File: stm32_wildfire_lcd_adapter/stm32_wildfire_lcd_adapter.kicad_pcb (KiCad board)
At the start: 2 copper layers, 30 x 30 mm, 3 parts, among them J1 Wildfire_40P_LCD, J2 STM32_40_LCD

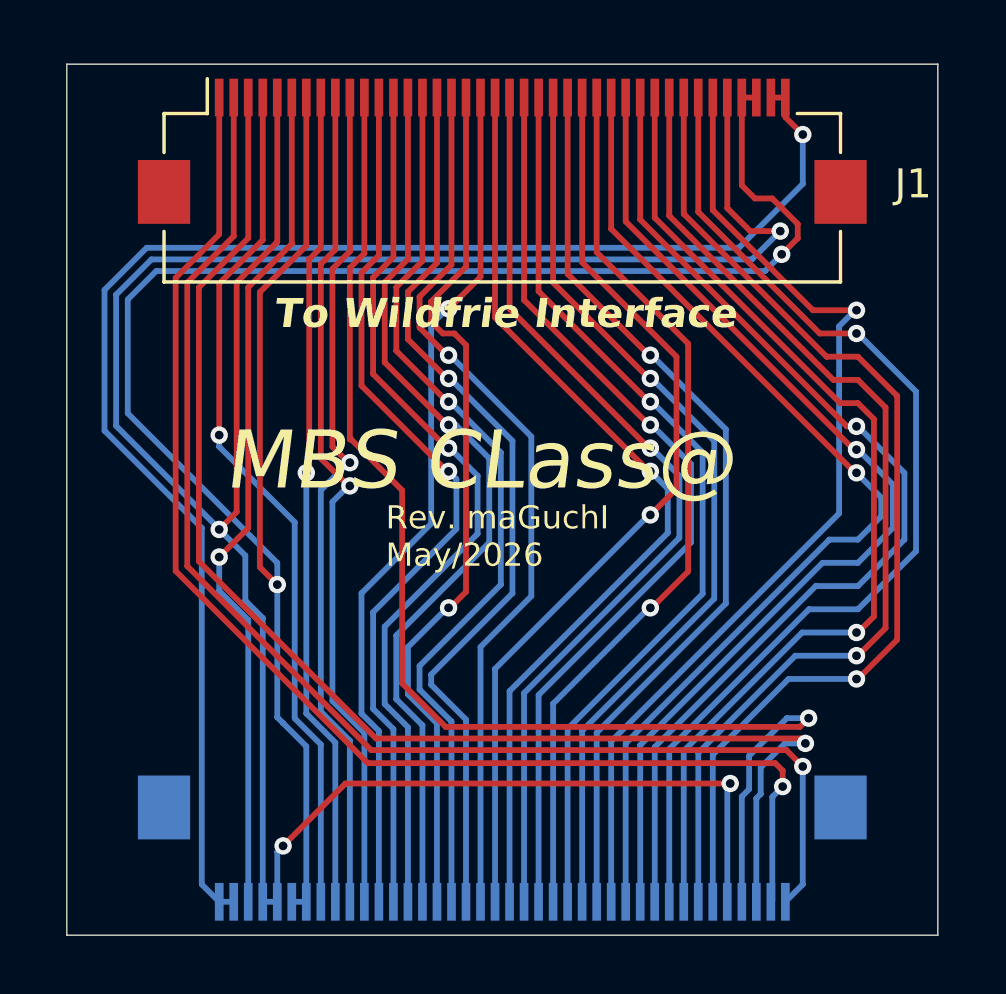
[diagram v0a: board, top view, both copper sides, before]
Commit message: fixing pinout error from wrong manual
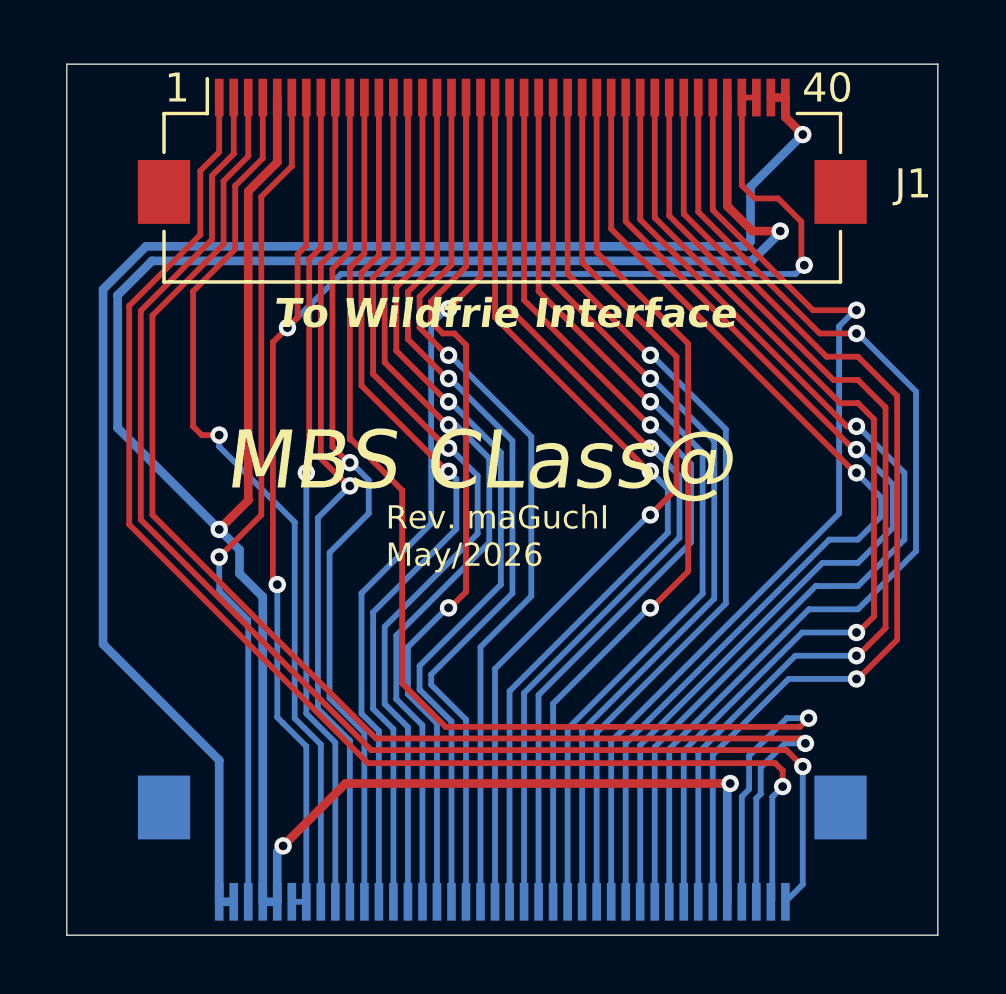
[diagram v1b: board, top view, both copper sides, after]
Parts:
- removed REF**: OSHW-Logo2_14.6x12mm_SilkScreen, Symbol:OSHW-Logo2_14.6x12mm_SilkScreen
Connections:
- J1 pad 10: /LCD_VSYNC -> /LCD_HSYNC
- J1 pad 9: /LCD_HSYNC -> /LCD_VSYNC
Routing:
- net /3V3: track 71.9 -> 55.5 mm, vias 2 -> 3
- net /CTP_SCL: track 45.4 -> 46.7 mm
- net /CTP_SDA: track 45.8 -> 47.1 mm
- net /CTP_INT: track 46.7 -> 48.1 mm
- net /CTP_RST: track 29.8 -> 30.9 mm
- net /LCD_HSYNC: track 29.1 -> 29.6 mm
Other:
- board text added: "1"
- board text added: "40"

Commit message: fixing fucking flipped fpc connector. how stupid of me!
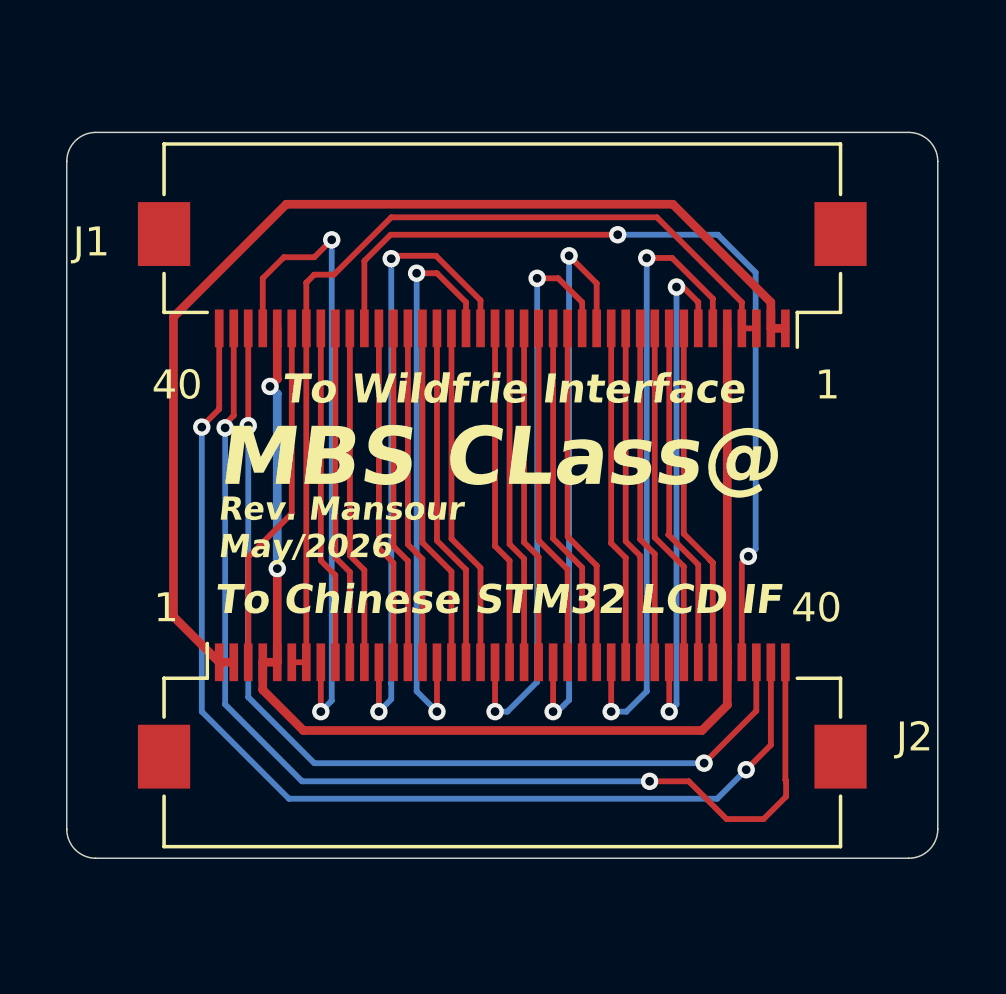
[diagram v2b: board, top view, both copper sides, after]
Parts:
- added REF**: OSHW-Logo2_14.6x12mm_SilkScreen, Symbol:OSHW-Logo2_14.6x12mm_SilkScreen, B.Cu at (105.2, 71.4)
- J2: moved to F.Cu
- moved J2 4.55 mm to (105.2, 79.0)
- moved J1 4.25 mm to (105.2, 63.8), turned to 180 degrees
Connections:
- J1 pad 1: /CTP_SCL -> /5V
- J1 pad 10: /LCD_HSYNC -> /LCD_R4
- J1 pad 11: /LCD_PCLK -> /LCD_R5
- J1 pad 12: /LCD_B7 -> /LCD_R6
- J1 pad 13: /LCD_B6 -> /LCD_R7
- J1 pad 14: /LCD_B5 -> /LCD_G0
- J1 pad 15: /LCD_B4 -> /LCD_G1
- J1 pad 16: /LCD_B3 -> /LCD_G2
- J1 pad 17: /LCD_B2 -> /LCD_G3
- J1 pad 18: /LCD_B1 -> /LCD_G4
- J1 pad 19: /LCD_B0 -> /LCD_G5
- J1 pad 2: /CTP_SDA -> /5V
- J1 pad 20: /LCD_G7 -> /LCD_G6
- J1 pad 21: /LCD_G6 -> /LCD_G7
- J1 pad 22: /LCD_G5 -> /LCD_B0
- J1 pad 23: /LCD_G4 -> /LCD_B1
- J1 pad 24: /LCD_G3 -> /LCD_B2
- J1 pad 25: /LCD_G2 -> /LCD_B3
- J1 pad 26: /LCD_G1 -> /LCD_B4
- J1 pad 27: /LCD_G0 -> /LCD_B5
- J1 pad 28: /LCD_R7 -> /LCD_B6
- J1 pad 29: /LCD_R6 -> /LCD_B7
- J1 pad 3: /CTP_INT -> /3V3
- J1 pad 30: /LCD_R5 -> /LCD_PCLK
- J1 pad 31: /LCD_R4 -> /LCD_HSYNC
- J1 pad 32: /LCD_R3 -> /LCD_VSYNC
- J1 pad 33: /LCD_R2 -> /LCD_DE
- J1 pad 34: /LCD_R1 -> /3V3
- J1 pad 35: /LCD_R0 -> /LCD_BL
- J1 pad 37: /3V3 -> /CTP_RST
- J1 pad 38: /3V3 -> /CTP_INT
- J1 pad 39: /5V -> /CTP_SDA
- J1 pad 4: /CTP_RST -> /3V3
- J1 pad 40: /5V -> /CTP_SCL
- J1 pad 6: /LCD_BL -> /LCD_R0
- J1 pad 7: /3V3 -> /LCD_R1
- J1 pad 8: /LCD_DE -> /LCD_R2
- J1 pad 9: /LCD_VSYNC -> /LCD_R3
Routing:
- net /GND: track 91.4 -> 43.1 mm, vias 4 -> 2
- net /LCD_R5: track 36.1 -> 11.7 mm, vias 1 -> 0
- net /LCD_R6: track 35.9 -> 11.7 mm, vias 1 -> 0
- net /LCD_R7: track 35.8 -> 11.7 mm, vias 1 -> 0
- net /3V3: track 55.5 -> 32.1 mm, vias 3 -> 0
- net /LCD_R2: track 35.4 -> 12.1 mm, vias 1 -> 0
- net /LCD_R3: track 35.2 -> 11.9 mm, vias 1 -> 0
- net /LCD_R4: track 35.0 -> 11.9 mm, vias 1 -> 0
- net /LCD_G7: track 32.5 -> 11.7 mm, vias 1 -> 0
- net /LCD_G6: track 32.4 -> 11.7 mm, vias 1 -> 0
- net /LCD_G5: track 32.3 -> 11.7 mm, vias 1 -> 0
- net /LCD_G4: track 32.0 -> 11.9 mm, vias 1 -> 0
- net /LCD_G3: track 31.9 -> 11.9 mm, vias 1 -> 0
- net /LCD_G2: track 31.9 -> 11.9 mm, vias 1 -> 0
- net /LCD_B5: track 31.4 -> 11.7 mm, vias 1 -> 0
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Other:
- board size 30 x 30 mm -> 30 x 25 mm
- board text added: "Rev. Mansour May/2026"
- board text removed: "Rev. maGuchI May/2026"
